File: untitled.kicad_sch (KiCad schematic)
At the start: 74 parts, among them U1 K210_C913414, U12 PCIE-67P42H, U4 XC6206P182MR_C347373, U5 GD25LQ128EWIGR, U6 TMI7003C, U7 SGM803-TXN3/TR_C5152602, U8 XC6206P302MR_C347375, X1 X322526MMB4SI

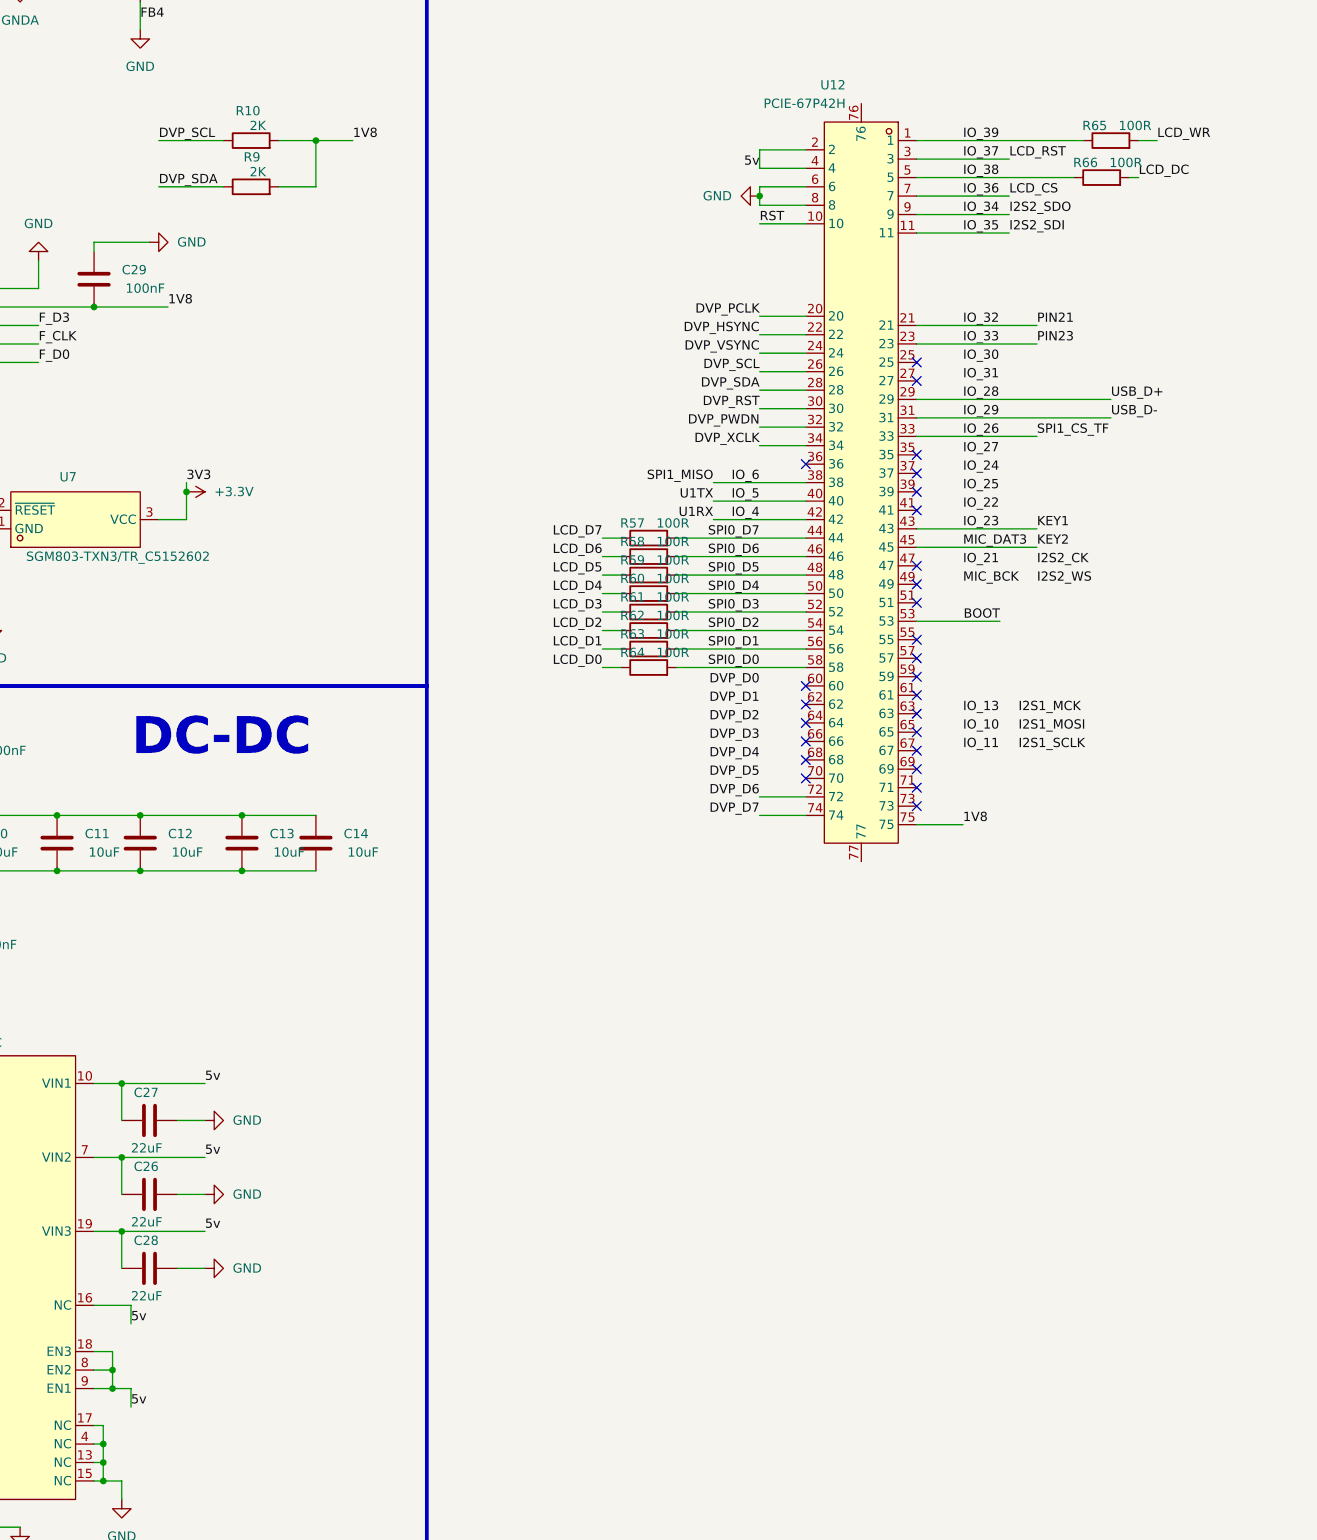
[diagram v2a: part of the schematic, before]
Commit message: m2 conector diagrama na placa principal
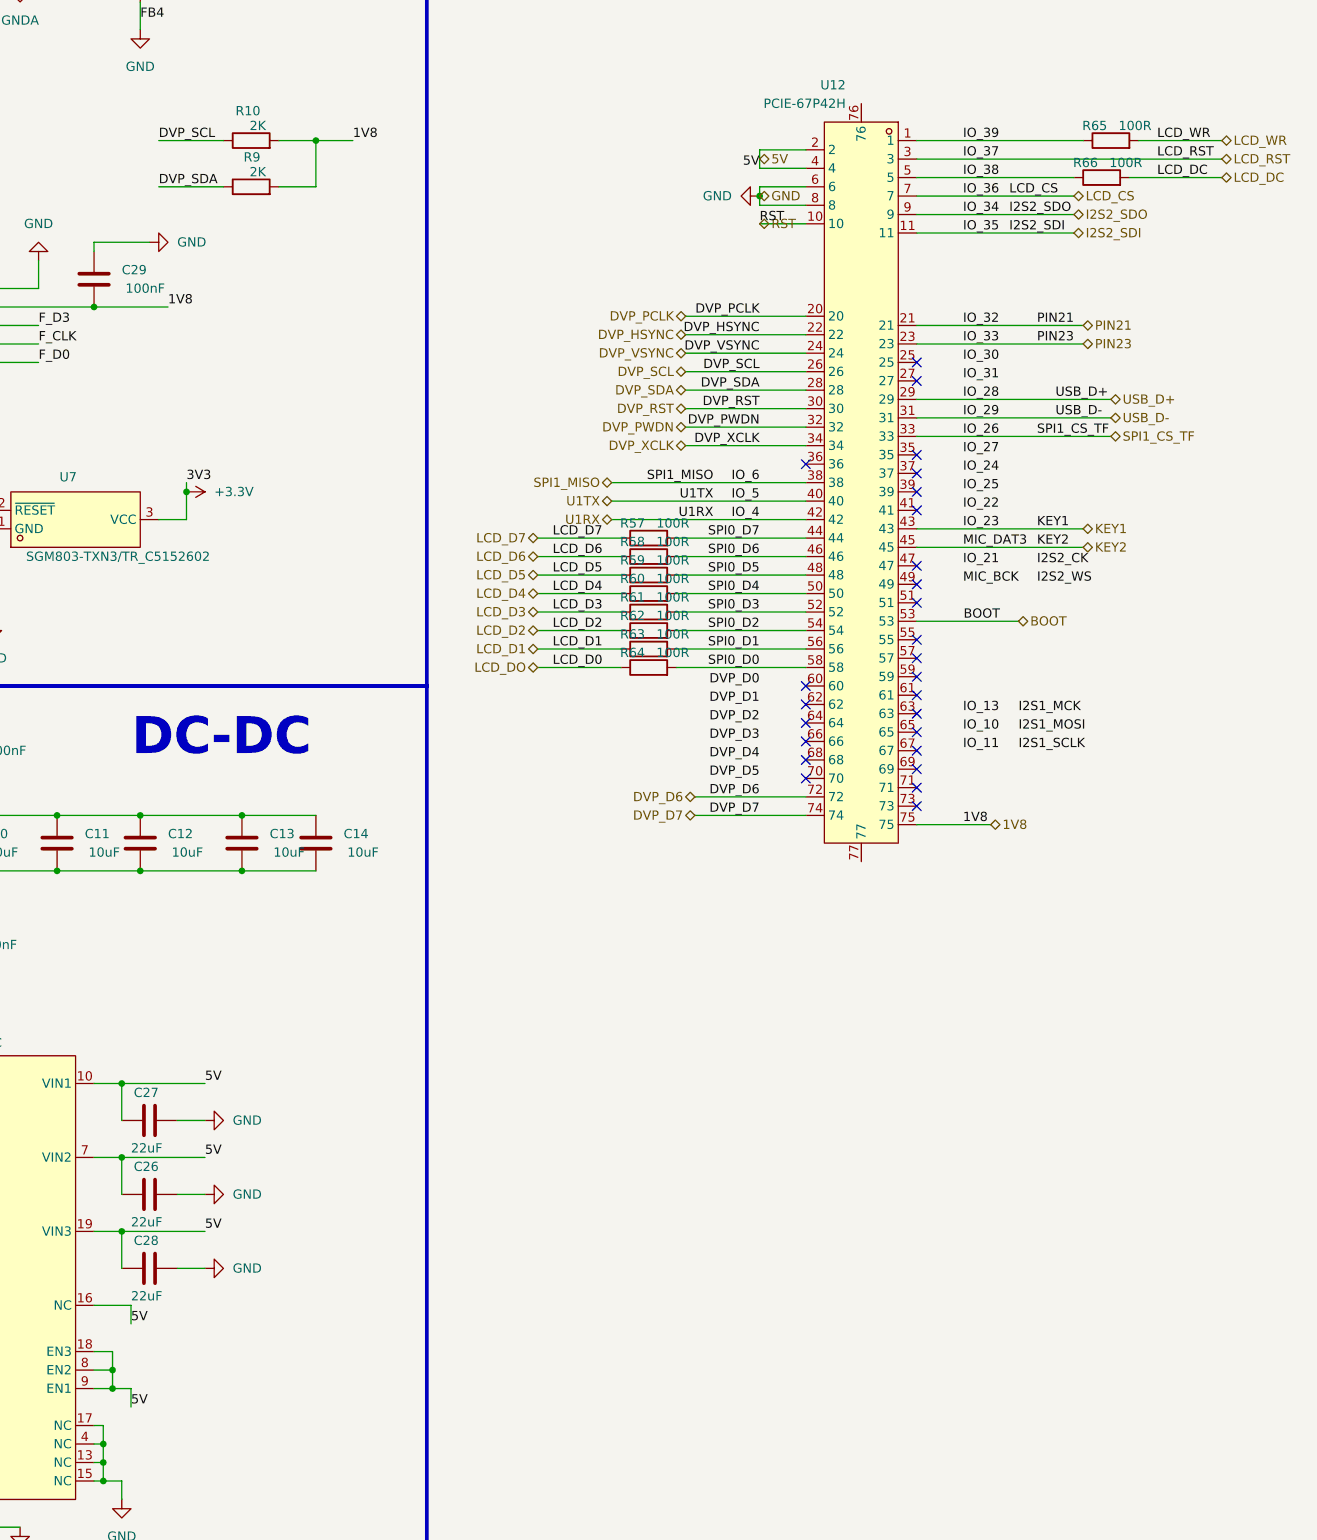
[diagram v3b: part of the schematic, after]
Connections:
- net 5v renamed 5V
- net IO_23 renamed KEY1
- net IO_26 renamed SPI1_CS_TF
- net IO_28 renamed USB_D+
- net IO_29 renamed USB_D-
- net IO_32 renamed PIN21
- net IO_33 renamed PIN23
- net IO_36 renamed LCD_CS
- net IO_37 renamed LCD_RST
- net IO_4 renamed U1RX
- net IO_5 renamed U1TX
- net IO_6 renamed SPI1_MISO
- net LCD_D0 renamed LCD_DO
